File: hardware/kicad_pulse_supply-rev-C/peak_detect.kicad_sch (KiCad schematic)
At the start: 62 parts, among them J2 OPT_PWR, U3 LTC6244CMS8

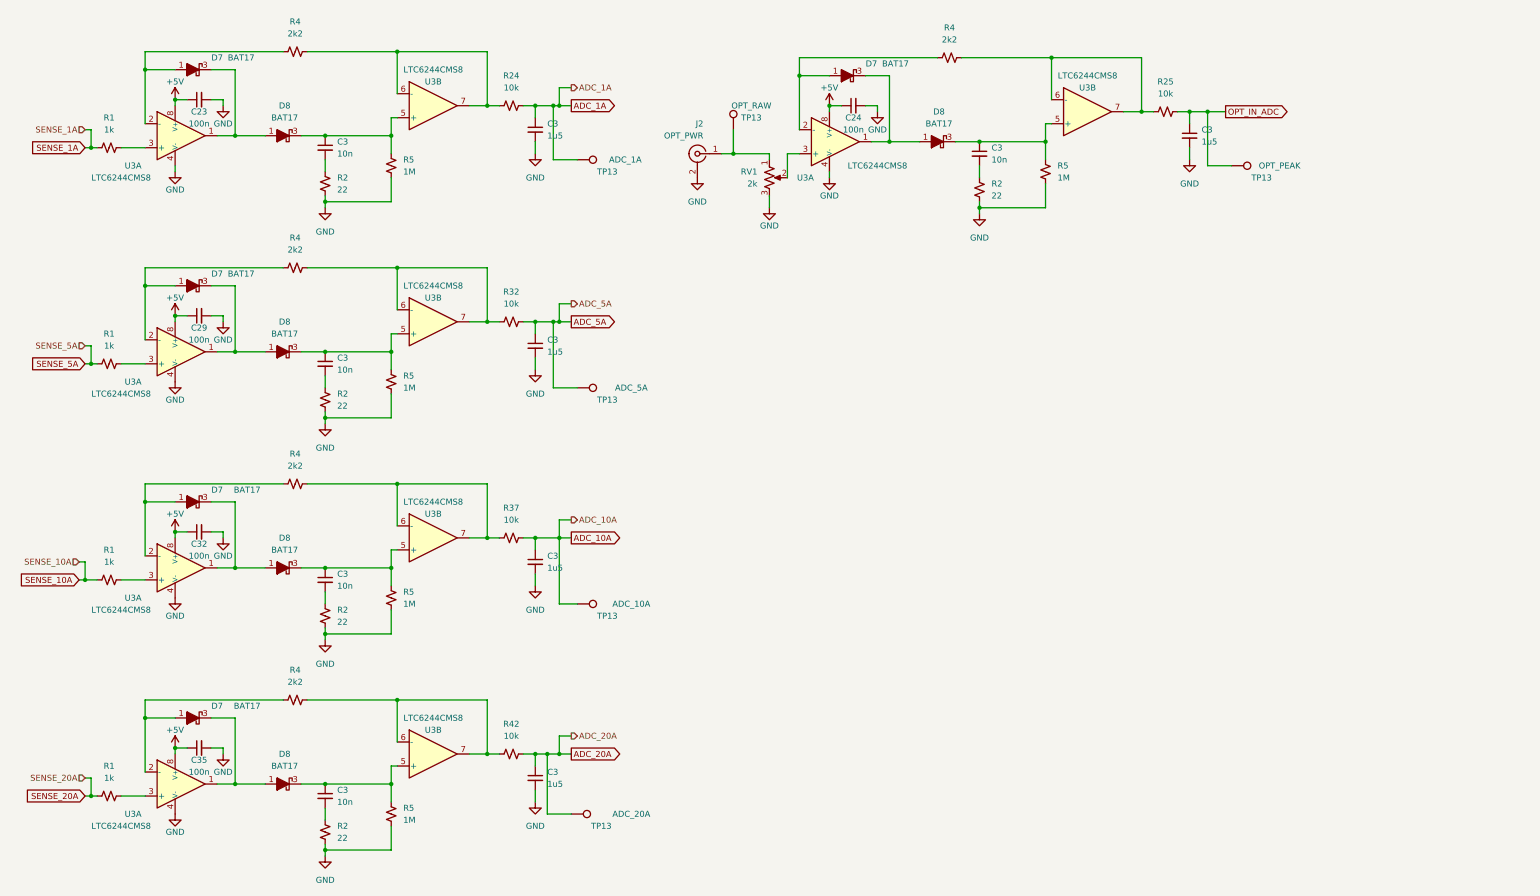
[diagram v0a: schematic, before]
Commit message: Refactored main loop to use Arduino Strings
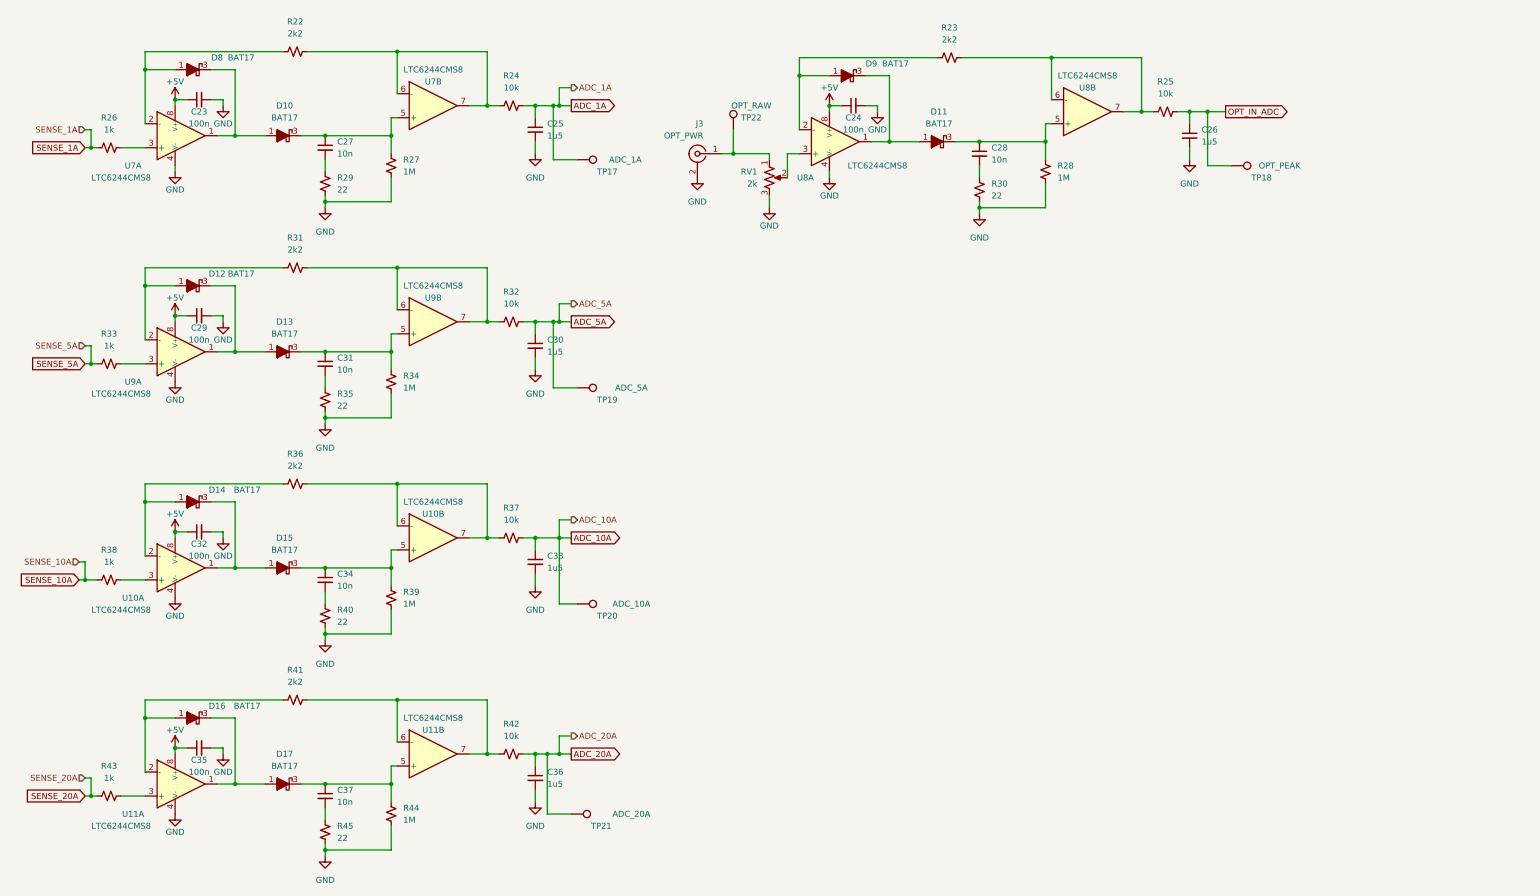
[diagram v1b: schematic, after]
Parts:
- renumbered C3 to C25, C3 to C26, C3 to C27, C3 to C28, C3 to C30, C3 to C31, C3 to C33, C3 to C34, C3 to C36, C3 to C37, D8 to D10, D8 to D11, D7 to D12, D8 to D13, D7 to D14, D8 to D15, D7 to D16, D8 to D17, D7 to D8, D7 to D9, J2 to J3, R4 to R22, R4 to R23, R1 to R26, R5 to R27, R5 to R28, R2 to R29, R2 to R30, R4 to R31, R1 to R33, R5 to R34, R2 to R35, R4 to R36, R1 to R38, R5 to R39, R2 to R40, R4 to R41, R1 to R43, R5 to R44, R2 to R45, TP13 to TP17, TP13 to TP18, TP13 to TP19, TP13 to TP20, TP13 to TP21, TP13 to TP22, U3 to U10, U3 to U11, U3 to U7, U3 to U8, U3 to U9

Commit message: hardware breakout boards added, pcb rev-c began
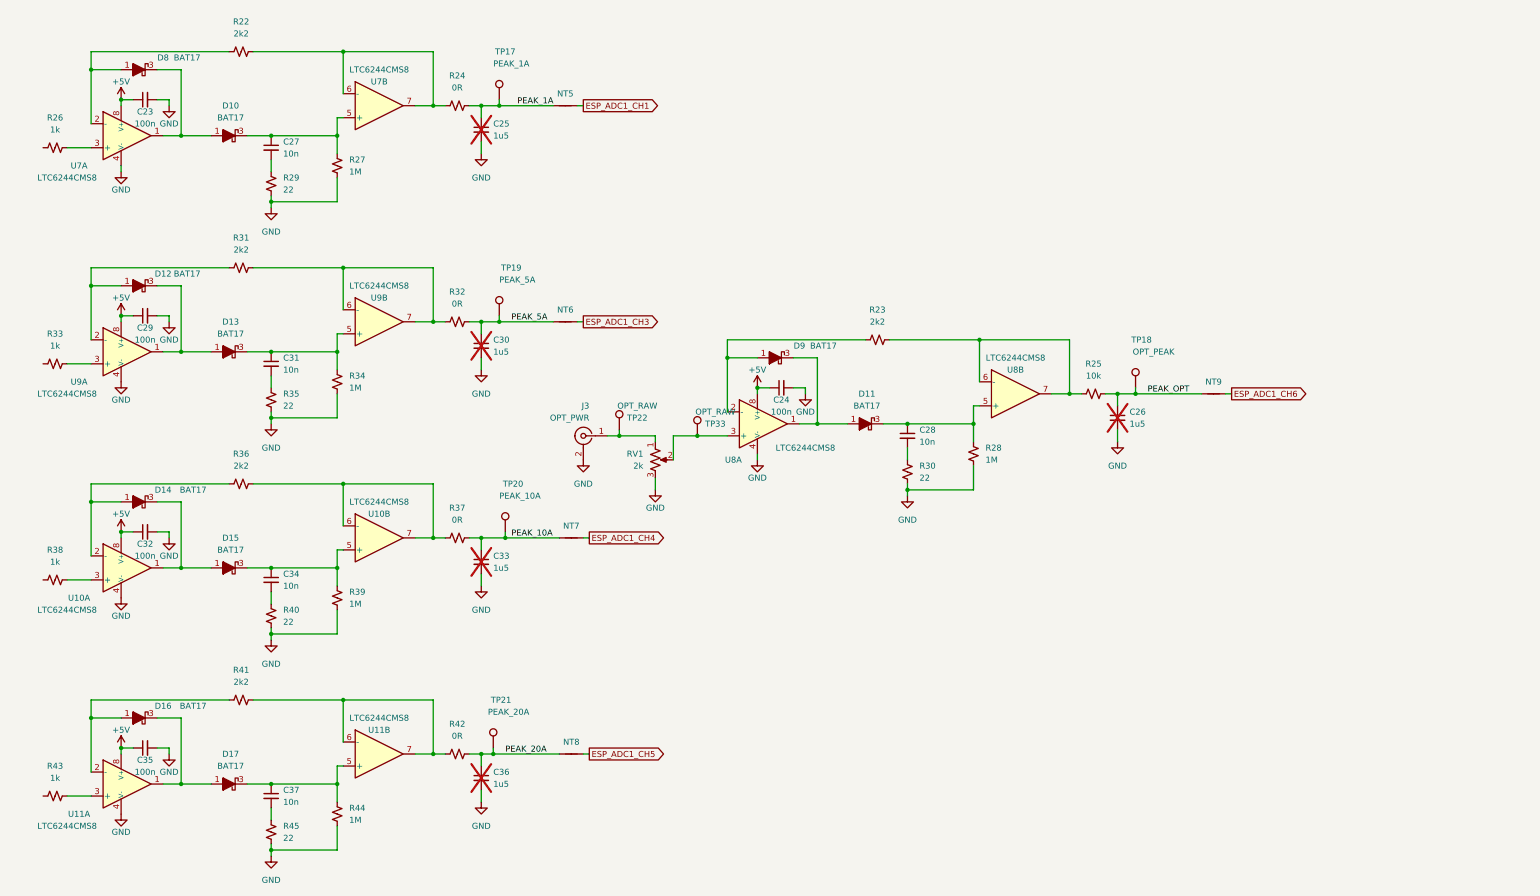
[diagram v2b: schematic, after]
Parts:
- added NT5, NT6, NT7, NT8, NT9: ~, symbol Device:NetTie_2
- added TP33: OPT_RAW, DW_Library:Keystone-1502-2, symbol Connector:TestPoint
- C25, C26, C30, C33, C36: now not fitted
- R24, R32, R37, R42: value 10k -> 0R
- TP17: value ADC_1A -> PEAK_1A
- TP19: value ADC_5A -> PEAK_5A
- TP20: value ADC_10A -> PEAK_10A
- TP21: value ADC_20A -> PEAK_20A
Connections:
- net at RV1.2, U8.3 (+): now also TP33.1
- net ADC_10A renamed PEAK_10A
- net PEAK_10A: now also NT7.1
- net ADC_1A renamed PEAK_1A
- net PEAK_1A: now also NT5.1
- net ADC_20A renamed PEAK_20A
- net PEAK_20A: now also NT8.1
- net ADC_5A renamed PEAK_5A
- net PEAK_5A: now also NT6.1
- net OPT_IN_ADC renamed PEAK_OPT
- net PEAK_OPT: now also NT9.1
- net SENSE_10A: no longer names the net of R38.1
- net SENSE_1A: no longer names the net of R26.1
- net SENSE_20A: no longer names the net of R43.1
- net SENSE_5A: no longer names the net of R33.1
- new net ESP_ADC1_CH1: NT5.2
- new net ESP_ADC1_CH3: NT6.2
- new net ESP_ADC1_CH4: NT7.2
- new net ESP_ADC1_CH5: NT8.2
- new net ESP_ADC1_CH6: NT9.2
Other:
- moved on the sheet: C23, C24, C27, C28, C29, C31, C32, C34, C35, C37, D10, D11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

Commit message: Rev C pcb complete, last commit before branching firmware for new board
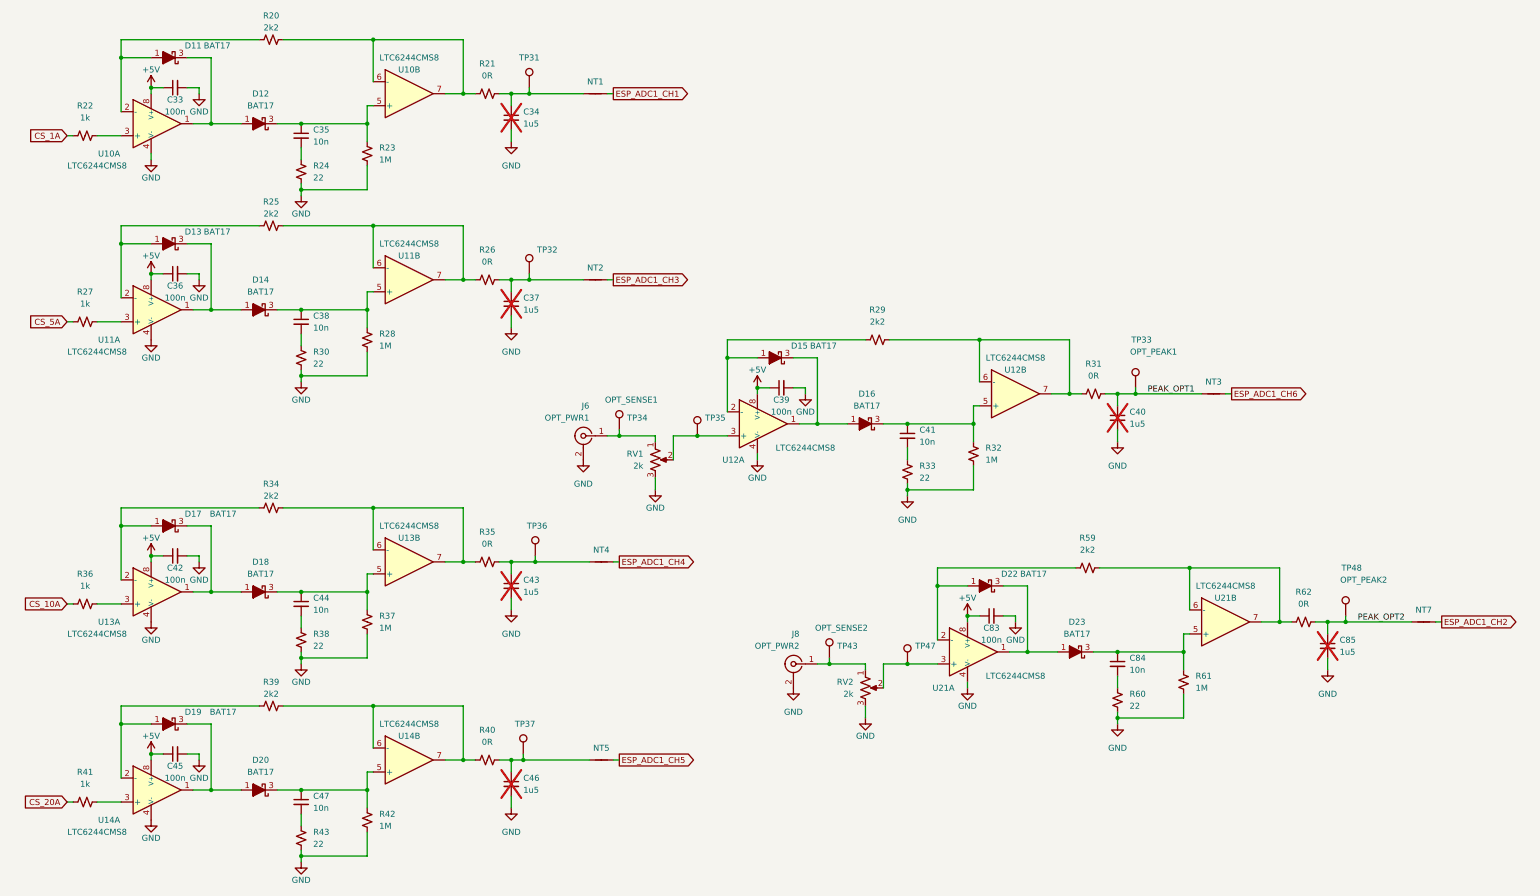
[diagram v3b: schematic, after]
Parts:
- added C83: 100n, Capacitor_SMD:C_0603_1608Metric, symbol Device:C_Small
- added C84: 10n, Capacitor_SMD:C_0603_1608Metric, symbol Device:C_Small
- added C85: 1u5, Capacitor_SMD:C_0603_1608Metric, symbol Device:C_Small
- added D22, D23: BAT17, PCM_Package_TO_SOT_SMD_AKL:SOT-23, symbol PCM_Diode_Schottky_AKL:BAT17
- added J8: OPT_PWR2, DW_Library:BNC_Molex_0731375003, symbol Connector:Conn_Coaxial
- added NT7: ~, DW_Library:Nettie-SMD-2-0.3mm, symbol Device:NetTie_2
- added R59: 2k2, Resistor_SMD:R_0603_1608Metric, symbol Device:R_Small_US
- added R60: 22, Resistor_SMD:R_0603_1608Metric, symbol Device:R_Small_US
- added R61: 1M, Resistor_SMD:R_0603_1608Metric, symbol Device:R_Small_US
- added R62: 0R, Resistor_SMD:R_0603_1608Metric, symbol Device:R_Small_US
- added RV2: 2k, Potentiometer_SMD:Potentiometer_Bourns_3214X_Vertical, symbol Device:R_Potentiometer_US
- added TP43: OPT_SENSE2, DW_Library:Keystone-1502-2, symbol Connector:TestPoint
- added TP47: OPT_RAW2, DW_Library:Keystone-1502-2, symbol Connector:TestPoint
- added TP48: OPT_PEAK2, DW_Library:Keystone-1502-2, symbol Connector:TestPoint
- added U21: LTC6244CMS8, PCM_Package_SO_AKL:MSOP-8_3x3mm_P0.65mm, symbol PCM_Amplifier_Operational_AKL:LTC6244CMS8
- C33: renamed from C23; footprint Capacitor_SMD:C_0603_1608Metric_Pad1.08x0.95mm_HandSolder -> Capacitor_SMD:C_0603_1608Metric
- C34: renamed from C25; footprint Capacitor_SMD:C_0603_1608Metric_Pad1.08x0.95mm_HandSolder -> Capacitor_SMD:C_0603_1608Metric
- C35: renamed from C27; footprint Capacitor_SMD:C_0603_1608Metric_Pad1.08x0.95mm_HandSolder -> Capacitor_SMD:C_0603_1608Metric
- C36: renamed from C29; footprint Capacitor_SMD:C_0603_1608Metric_Pad1.08x0.95mm_HandSolder -> Capacitor_SMD:C_0603_1608Metric
- C37: renamed from C30; footprint Capacitor_SMD:C_0603_1608Metric_Pad1.08x0.95mm_HandSolder -> Capacitor_SMD:C_0603_1608Metric
- C38: renamed from C31; footprint Capacitor_SMD:C_0603_1608Metric_Pad1.08x0.95mm_HandSolder -> Capacitor_SMD:C_0603_1608Metric
- C39: renamed from C24; footprint Capacitor_SMD:C_0603_1608Metric_Pad1.08x0.95mm_HandSolder -> Capacitor_SMD:C_0603_1608Metric
- C40: renamed from C26; footprint Capacitor_SMD:C_0603_1608Metric_Pad1.08x0.95mm_HandSolder -> Capacitor_SMD:C_0603_1608Metric
- C41: renamed from C28; footprint Capacitor_SMD:C_0603_1608Metric_Pad1.08x0.95mm_HandSolder -> Capacitor_SMD:C_0603_1608Metric
- C42: renamed from C32; footprint Capacitor_SMD:C_0603_1608Metric_Pad1.08x0.95mm_HandSolder -> Capacitor_SMD:C_0603_1608Metric
- C43: renamed from C33; footprint Capacitor_SMD:C_0603_1608Metric_Pad1.08x0.95mm_HandSolder -> Capacitor_SMD:C_0603_1608Metric
- C44: renamed from C34; footprint Capacitor_SMD:C_0603_1608Metric_Pad1.08x0.95mm_HandSolder -> Capacitor_SMD:C_0603_1608Metric
- C45: renamed from C35; footprint Capacitor_SMD:C_0603_1608Metric_Pad1.08x0.95mm_HandSolder -> Capacitor_SMD:C_0603_1608Metric
- C46: renamed from C36; footprint Capacitor_SMD:C_0603_1608Metric_Pad1.08x0.95mm_HandSolder -> Capacitor_SMD:C_0603_1608Metric
- C47: renamed from C37; footprint Capacitor_SMD:C_0603_1608Metric_Pad1.08x0.95mm_HandSolder -> Capacitor_SMD:C_0603_1608Metric
- D11: renamed from D8; footprint Package_TO_SOT_SMD:SOT-23 -> PCM_Package_TO_SOT_SMD_AKL:SOT-23
- D12: renamed from D10; footprint Package_TO_SOT_SMD:SOT-23 -> PCM_Package_TO_SOT_SMD_AKL:SOT-23
- D13: renamed from D12; footprint Package_TO_SOT_SMD:SOT-23 -> PCM_Package_TO_SOT_SMD_AKL:SOT-23
- D14: renamed from D13; footprint Package_TO_SOT_SMD:SOT-23 -> PCM_Package_TO_SOT_SMD_AKL:SOT-23
- D15: renamed from D9; footprint Package_TO_SOT_SMD:SOT-23 -> PCM_Package_TO_SOT_SMD_AKL:SOT-23
- D16: renamed from D11; footprint Package_TO_SOT_SMD:SOT-23 -> PCM_Package_TO_SOT_SMD_AKL:SOT-23
- D17: renamed from D14; footprint Package_TO_SOT_SMD:SOT-23 -> PCM_Package_TO_SOT_SMD_AKL:SOT-23
- D18: renamed from D15; footprint Package_TO_SOT_SMD:SOT-23 -> PCM_Package_TO_SOT_SMD_AKL:SOT-23
- D19: renamed from D16; footprint Package_TO_SOT_SMD:SOT-23 -> PCM_Package_TO_SOT_SMD_AKL:SOT-23
- D20: renamed from D17; footprint Package_TO_SOT_SMD:SOT-23 -> PCM_Package_TO_SOT_SMD_AKL:SOT-23
- J6: renamed from J3; value OPT_PWR -> OPT_PWR1
- NT1: renamed from NT5; footprint (none) -> DW_Library:Nettie-SMD-2-0.3mm
- NT2: renamed from NT6; footprint (none) -> DW_Library:Nettie-SMD-2-0.3mm
- NT3: renamed from NT9; footprint (none) -> DW_Library:Nettie-SMD-2-0.3mm
- NT4: renamed from NT7; footprint (none) -> DW_Library:Nettie-SMD-2-0.3mm
- NT5: renamed from NT8; footprint (none) -> DW_Library:Nettie-SMD-2-0.3mm
- R20: renamed from R22; footprint Resistor_SMD:R_0603_1608Metric_Pad0.98x0.95mm_HandSolder -> Resistor_SMD:R_0603_1608Metric
- R21: renamed from R24; footprint Resistor_SMD:R_0603_1608Metric_Pad0.98x0.95mm_HandSolder -> Resistor_SMD:R_0603_1608Metric
- R22: renamed from R26; footprint Resistor_SMD:R_0603_1608Metric_Pad0.98x0.95mm_HandSolder -> Resistor_SMD:R_0603_1608Metric
- R23: renamed from R27; footprint Resistor_SMD:R_0603_1608Metric_Pad0.98x0.95mm_HandSolder -> Resistor_SMD:R_0603_1608Metric
- R24: renamed from R29; footprint Resistor_SMD:R_0603_1608Metric_Pad0.98x0.95mm_HandSolder -> Resistor_SMD:R_0603_1608Metric
- R25: renamed from R31; footprint Resistor_SMD:R_0603_1608Metric_Pad0.98x0.95mm_HandSolder -> Resistor_SMD:R_0603_1608Metric
- R26: renamed from R32; footprint Resistor_SMD:R_0603_1608Metric_Pad0.98x0.95mm_HandSolder -> Resistor_SMD:R_0603_1608Metric
- R27: renamed from R33; footprint Resistor_SMD:R_0603_1608Metric_Pad0.98x0.95mm_HandSolder -> Resistor_SMD:R_0603_1608Metric
- R28: renamed from R34; footprint Resistor_SMD:R_0603_1608Metric_Pad0.98x0.95mm_HandSolder -> Resistor_SMD:R_0603_1608Metric
- R29: renamed from R23; footprint Resistor_SMD:R_0603_1608Metric_Pad0.98x0.95mm_HandSolder -> Resistor_SMD:R_0603_1608Metric
- R30: renamed from R35; footprint Resistor_SMD:R_0603_1608Metric_Pad0.98x0.95mm_HandSolder -> Resistor_SMD:R_0603_1608Metric
- R31: renamed from R25; value 10k -> 0R; footprint Resistor_SMD:R_0603_1608Metric_Pad0.98x0.95mm_HandSolder -> Resistor_SMD:R_0603_1608Metric
- R32: renamed from R28; footprint Resistor_SMD:R_0603_1608Metric_Pad0.98x0.95mm_HandSolder -> Resistor_SMD:R_0603_1608Metric
- R33: renamed from R30; footprint Resistor_SMD:R_0603_1608Metric_Pad0.98x0.95mm_HandSolder -> Resistor_SMD:R_0603_1608Metric
- R34: renamed from R36; footprint Resistor_SMD:R_0603_1608Metric_Pad0.98x0.95mm_HandSolder -> Resistor_SMD:R_0603_1608Metric
- R35: renamed from R37; footprint Resistor_SMD:R_0603_1608Metric_Pad0.98x0.95mm_HandSolder -> Resistor_SMD:R_0603_1608Metric
- R36: renamed from R38; footprint Resistor_SMD:R_0603_1608Metric_Pad0.98x0.95mm_HandSolder -> Resistor_SMD:R_0603_1608Metric
- R37: renamed from R39; footprint Resistor_SMD:R_0603_1608Metric_Pad0.98x0.95mm_HandSolder -> Resistor_SMD:R_0603_1608Metric
- R38: renamed from R40; footprint Resistor_SMD:R_0603_1608Metric_Pad0.98x0.95mm_HandSolder -> Resistor_SMD:R_0603_1608Metric
- R39: renamed from R41; footprint Resistor_SMD:R_0603_1608Metric_Pad0.98x0.95mm_HandSolder -> Resistor_SMD:R_0603_1608Metric
- R40: renamed from R42; footprint Resistor_SMD:R_0603_1608Metric_Pad0.98x0.95mm_HandSolder -> Resistor_SMD:R_0603_1608Metric
- R41: renamed from R43; footprint Resistor_SMD:R_0603_1608Metric_Pad0.98x0.95mm_HandSolder -> Resistor_SMD:R_0603_1608Metric
- R42: renamed from R44; footprint Resistor_SMD:R_0603_1608Metric_Pad0.98x0.95mm_HandSolder -> Resistor_SMD:R_0603_1608Metric
- R43: renamed from R45; footprint Resistor_SMD:R_0603_1608Metric_Pad0.98x0.95mm_HandSolder -> Resistor_SMD:R_0603_1608Metric
- TP33: renamed from TP18; value OPT_PEAK -> OPT_PEAK1
- TP34: renamed from TP22; value OPT_RAW -> OPT_SENSE1
- TP35: renamed from TP33; value OPT_RAW -> OPT_RAW1
- U10: renamed from U7; footprint Package_SO:MSOP-8_3x3mm_P0.65mm -> PCM_Package_SO_AKL:MSOP-8_3x3mm_P0.65mm
- U11: renamed from U9; footprint Package_SO:MSOP-8_3x3mm_P0.65mm -> PCM_Package_SO_AKL:MSOP-8_3x3mm_P0.65mm
- U12: renamed from U8; footprint Package_SO:MSOP-8_3x3mm_P0.65mm -> PCM_Package_SO_AKL:MSOP-8_3x3mm_P0.65mm
- U13: renamed from U10; footprint Package_SO:MSOP-8_3x3mm_P0.65mm -> PCM_Package_SO_AKL:MSOP-8_3x3mm_P0.65mm
- U14: renamed from U11; footprint Package_SO:MSOP-8_3x3mm_P0.65mm -> PCM_Package_SO_AKL:MSOP-8_3x3mm_P0.65mm
- renumbered TP17 to TP31, TP19 to TP32, TP20 to TP36, TP21 to TP37
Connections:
- net +5V: now also C83.1, U21.8 (V+)
- net GND: now also C83.2, C85.2, J8.2 (Ext), R60.2, R61.2, RV2.3, U21.4 (V-)
- net CS_20A: now reaches R41.1
- net CS_1A: now reaches R22.1
- net CS_5A: now reaches R27.1
- net CS_10A: now reaches R36.1
- net PEAK_10A: no longer names the net of C43.1, NT4.1, R35.2, TP36.1
- net PEAK_1A: no longer names the net of C34.1, NT1.1, R21.2, TP31.1
- net PEAK_20A: no longer names the net of C46.1, NT5.1, R40.2, TP37.1
- net PEAK_5A: no longer names the net of C37.1, NT2.1, R26.2, TP32.1
- net PEAK_OPT renamed PEAK_OPT1
- new net: D22.3 (K), D23.1 (A), U21.1
- new net: D22.1 (A), R59.1, U21.2 (-)
- new net: RV2.2, TP47.1, U21.3 (+)
- new net: C84.1, D23.3 (K), R61.1, U21.5 (+)
- new net: R59.2, R62.1, U21.6 (-), U21.7
- new net: J8.1 (In), RV2.1, TP43.1
- new net: C84.2, R60.1
- new net ESP_ADC1_CH2: NT7.2
- new net PEAK_OPT2: C85.1, NT7.1, R62.2, TP48.1
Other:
- moved on the sheet: C33, C34, C35, C36, C37, C38, C42, C43, C44, C45, C46, C47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
